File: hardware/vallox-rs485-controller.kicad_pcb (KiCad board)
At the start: 0 parts

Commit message: hw(pcb): rev A placement on a 104 x 66 mm board, not yet routed
The board file was empty. All 60 schematic parts are now on the top side,
placed from the netlist with KiCad's bundled pcbnew Python (KiCad closed):
the MCP server had no pcb_write tools this session and the file-based MCP
transfer tool is the one the workspace forbids. Every footprint carries its
symbol UUID as path, so a GUI F8 should reconcile to no changes.

Floor plan: display glass reserve top-left with the four buttons centred
under it and the LEDs beside it; FPC connector on the glass's short edge;
ESP32 module top-right with its antenna 6 mm over the edge, the position the
Espressif hardware design guide recommends; terminal block and USB-C flush
with the right edge so all field wiring enters from one wall; buck in the
bottom-right corner, RS-485 front end between terminal and module.

kicad-cli drc --severity-all --schematic-parity: 0 errors, 7 warnings
(silkscreen of edge-mounted U1/J1/J2 crossing the edge; U1 thermal vias
widened from 0.2 to 0.3 mm drill to meet the project's min-hole rule),
parity clean apart from the four intentional mounting holes, 138 unconnected
items because nothing is routed. Parity caught two build mistakes on the way:
footprints written without their library nickname, and TP1/TP2/JP1 symbols
not excluded from BOM while their footprints are — the symbols now say
in_bom no, ERC unchanged.

CI's DRC step will stay red on this branch until the board is routed:
--exit-code-violations also counts unconnected items (verified locally).
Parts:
- added C1: 220u/35V, Capacitor_SMD:CP_Elec_8x10.5, F.Cu at (80.0, 58.5)
- added C10: 10u, Capacitor_SMD:C_0603_1608Metric, F.Cu at (80.3, 2.20)
- added C11: 100n, Capacitor_SMD:C_0603_1608Metric, F.Cu at (75.5, 2.20)
- added C12: 100n, Capacitor_SMD:C_0603_1608Metric, F.Cu at (80.3, 13.4)
- added C13: 1u, Capacitor_SMD:C_0603_1608Metric, F.Cu at (80.3, 7.80)
- added C2: 2.2u/50V, Capacitor_SMD:C_0805_2012Metric, F.Cu at (79.8, 50.2)
- added C3: 100n, Capacitor_SMD:C_0603_1608Metric, F.Cu at (85.6, 47.6)
- added C4: 22u/10V, Capacitor_SMD:C_0805_2012Metric, F.Cu at (69.0, 48.6)
- added C5: 22u/10V, Capacitor_SMD:C_0805_2012Metric, F.Cu at (69.0, 52.2)
- added C7: 10u, Capacitor_SMD:C_0603_1608Metric, F.Cu at (72.8, 42.5)
- added C8: 100n, Capacitor_SMD:C_0603_1608Metric, F.Cu at (84.8, 38.6)
- added C9: 1u, Capacitor_SMD:C_0603_1608Metric, F.Cu at (73.5, 24.5)
- added D1: SS34, Diode_SMD:D_SMA, F.Cu at (89.9, 59.5)
- added D2: SM712, Package_TO_SOT_SMD:SOT-23, F.Cu at (90.8, 36.0)
- added D3: SS34, Diode_SMD:D_SMA, F.Cu at (89.5, 32.4)
- added D4: PWR, LED_SMD:LED_0603_1608Metric, F.Cu at (63.8, 10.0)
- added D5: FAULT, LED_SMD:LED_0603_1608Metric, F.Cu at (63.8, 18.0)
- added D6: BUS, LED_SMD:LED_0603_1608Metric, F.Cu at (63.8, 14.0)
- added F1: 100mA/60V, Fuse:Fuse_1812_4532Metric, F.Cu at (90.2, 45.6)
- added F2: 100mA/60V, Fuse:Fuse_1812_4532Metric, F.Cu at (90.2, 39.9)
- added H1: M3, MountingHole:MountingHole_3.2mm_M3, F.Cu at (3.50, 3.50)
- added H2: M3, MountingHole:MountingHole_3.2mm_M3, F.Cu at (3.50, 62.5)
- added H3: M3, MountingHole:MountingHole_3.2mm_M3, F.Cu at (100.5, 62.5)
- added H4: M3, MountingHole:MountingHole_3.2mm_M3, F.Cu at (70.0, 3.50)
- added J1: + - A B M, TerminalBlock_Phoenix:TerminalBlock_Phoenix_MKDS-1,5-5-5.08_1x05_P5.08mm_Horizontal, F.Cu at (99.4, 55.5)
- added J2: TYPE-C-31-M-12, Connector_USB:USB_C_Receptacle_HRO_TYPE-C-31-M-12, F.Cu at (100.3, 26.0)
- added J3: HS20HS072RX, Connector_FFC-FPC:Hirose_FH12-12S-0.5SH_1x12-1MP_P0.50mm_Horizontal, F.Cu at (67.0, 26.1)
- added JP1: TERM, Jumper:SolderJumper-2_P1.3mm_Open_RoundedPad1.0x1.5mm, F.Cu at (82.6, 35.0)
- added L1: 22uH, Inductor_SMD:L_Changjiang_FNR6045S, F.Cu at (74.5, 50.2)
- added Q1: AO3400A, Package_TO_SOT_SMD:SOT-23, F.Cu at (73.5, 30.5)
- added R1: 100k, Resistor_SMD:R_0603_1608Metric, F.Cu at (89.0, 52.5)
- added R10: 10k, Resistor_SMD:R_0603_1608Metric, F.Cu at (73.5, 22.3)
- added R11: 27R, Resistor_SMD:R_1206_3216Metric, F.Cu at (73.5, 34.2)
- added R12: 100R, Resistor_SMD:R_0603_1608Metric, F.Cu at (77.5, 29.5)
- added R13: 10k, Resistor_SMD:R_0603_1608Metric, F.Cu at (77.5, 31.5)
- added R14: 5.1k, Resistor_SMD:R_0603_1608Metric, F.Cu at (92.5, 28.5)
- added R15: 5.1k, Resistor_SMD:R_0603_1608Metric, F.Cu at (92.5, 23.5)
- added R19: 10k, Resistor_SMD:R_0603_1608Metric, F.Cu at (80.3, 5.00)
- added R2: 15k, Resistor_SMD:R_0603_1608Metric, F.Cu at (89.0, 50.8)
- added R20: 1k, Resistor_SMD:R_0603_1608Metric, F.Cu at (67.3, 10.0)
- added R21: 10k, Resistor_SMD:R_0603_1608Metric, F.Cu at (73.5, 26.7)
- added R22: 10k, Resistor_SMD:R_0603_1608Metric, F.Cu at (80.3, 10.6)
- added R23: 1.5k, Resistor_SMD:R_0603_1608Metric, F.Cu at (27.5, 58.5)
- added R24: 3.3k, Resistor_SMD:R_0603_1608Metric, F.Cu at (40.5, 58.5)
- added R25: 6.8k, Resistor_SMD:R_0603_1608Metric, F.Cu at (53.5, 58.5)
- added R26: 1k, Resistor_SMD:R_0603_1608Metric, F.Cu at (67.3, 18.0)
- added R27: 1k, Resistor_SMD:R_0603_1608Metric, F.Cu at (67.3, 14.0)
- added R3: 100k, Resistor_SMD:R_0603_1608Metric, F.Cu at (89.0, 55.9)
- added R4: 13.3k, Resistor_SMD:R_0603_1608Metric, F.Cu at (89.0, 54.2)
- added R5: 120R DNP, Resistor_SMD:R_0603_1608Metric, F.Cu at (79.2, 35.0)
- added R6: 1k DNP, Resistor_SMD:R_0603_1608Metric, F.Cu at (78.4, 38.6)
- added R7: 1k DNP, Resistor_SMD:R_0603_1608Metric, F.Cu at (81.6, 38.6)
- added R8: 10k, Resistor_SMD:R_0603_1608Metric, F.Cu at (75.5, 7.60)
- added R9: 10k, Resistor_SMD:R_0603_1608Metric, F.Cu at (75.5, 10.4)
- added SW1: -, Button_Switch_SMD:SW_SPST_PTS645Sx43SMTR92, F.Cu at (14.5, 52.0)
- added SW2: +, Button_Switch_SMD:SW_SPST_PTS645Sx43SMTR92, F.Cu at (27.5, 52.0)
- added SW3: OK, Button_Switch_SMD:SW_SPST_PTS645Sx43SMTR92, F.Cu at (40.5, 52.0)
- added SW4: BACK, Button_Switch_SMD:SW_SPST_PTS645Sx43SMTR92, F.Cu at (53.5, 52.0)
- added TP1: EN, TestPoint:TestPoint_Pad_1.0x1.0mm, F.Cu at (75.5, 4.80)
- added TP2: BOOT, TestPoint:TestPoint_Pad_1.0x1.0mm, F.Cu at (77.6, 13.0)
- added U1: ESP32-C3-WROOM-02-N4, RF_Module:ESP32-C3-WROOM-02, F.Cu at (92.0, 7.10)
- added U2: TPS54202DDC, Package_TO_SOT_SMD:SOT-23-6, F.Cu at (83.5, 50.2)
- added U3: ME6211C33M5G-N, Package_TO_SOT_SMD:SOT-23-5, F.Cu at (69.0, 43.5)
- added U4: THVD1400DR, Package_SO:SOIC-8_3.9x4.9mm_P1.27mm, F.Cu at (82.5, 42.8)
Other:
- board outline added: 104 x 66 mm
- copper layers 0 -> 2
- board text added: "+"
- board text added: "-"
- board text added: "A"
- board text added: "B"
- board text added: "BACK"
- board text added: "BUS"
- board text added: "FAULT"
- board text added: "FPC tail assumed to exit the right (short) edge toward J3 - verify from the display drawing."
- board text added: "HS20HS072RX glass 51.8 x 36.2 mm - component-free area (glass rests on the board)."
- board text added: "Keep enclosure metal >= 15 mm from the antenna."
- board text added: "M"
- board text added: "OK"
- board text added: "PWR"
- board text added: "U1 antenna overhangs the board edge by 6 mm (Espressif HDG preferred position)."
- board text added: "VALLOX RS-485 CONTROLLER rev A"
- board text added: "mironet.fi github.com/Miroeilola/vallox-rs485-controller"

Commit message: hw(display): place DS1 glass from the shared library, move the LEDs off the FPC tail
The shared library now has an own model of the HS20HS072RX and a pad-less
footprint for it, so the reserved rectangle becomes a real part on the board.
The first render with the glass in place showed the 20.6 mm wide tail root
lying across the FAULT LED and its legend; the LED column moves up three
millimetres and one mounting hole moves left to make room. DRC and schematic
parity unchanged (0 errors; the four holes are the only extras), 138 items
still unrouted.

Also fixes the model path on the placed footprint: the library convention
resolved relative to the KiCad project directory, which in this layout is
hardware/, not the repository root where the submodule lives.
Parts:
- added DS1: HS20HS072RX, mironet:LCD_2.0in_HSD_HS20HS072RX_FPC-12P-0.5mm, F.Cu at (33.9, 26.1)
- moved D5 4.20 mm to (63.8, 13.8)
- moved R26 4.20 mm to (67.3, 13.8)
- moved H4 4.00 mm to (66.0, 3.50)
- moved D6 3.20 mm to (63.8, 10.8)
- moved R27 3.20 mm to (67.3, 10.8)
- moved D4 2.20 mm to (63.8, 7.80)
- moved R20 2.20 mm to (67.3, 7.80)
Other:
- board text added: "DS1 glass rests on the board; tail contact side unverified (drawing: viewer side) - decides whether J3 turns 180 deg"
- board text removed: "FPC tail assumed to exit the right (short) edge toward J3 - verify from the display drawing."
- board text removed: "HS20HS072RX glass 51.8 x 36.2 mm - component-free area (glass rests on the board)."
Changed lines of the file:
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@@
 	(footprint "Resistor_SMD:R_0603_1608Metric"
 		(layer "F.Cu")
-		(at 67.3 18)
+		(at 67.3 13.8)
 		(descr "Resistor SMD 0603 (1608 Metric), square (rectangular) end terminal, IPC-7351 nominal, (Body size source: IPC-SM-782 page 72, https://www.pcb-3d.com/wordpress/wp-content/uploads/ipc-sm-782a_amendment_1_and_2.pdf)")
 		(tags "resistor")
 		(property "Reference" "R26"
-			(at 0 -1.7036 0)
+			(at 0 1.7036 0)
 			(layer "F.SilkS")
 			(effects
@@
 	(footprint "Resistor_SMD:R_0603_1608Metric"
 		(layer "F.Cu")
-		(at 67.3 14)
+		(at 67.3 10.8)
 		(descr "Resistor SMD 0603 (1608 Metric), square (rectangular) end terminal, IPC-7351 nominal, (Body size source: IPC-SM-782 page 72, https://www.pcb-3d.com/wordpress/wp-content/uploads/ipc-sm-782a_amendment_1_and_2.pdf)")
 		(tags "resistor")
@@
 		(tags "capacitor")
 		(property "Reference" "C11"
-			(at 2.4536 0 90)
+			(at 3.036905 0 0)
 			(layer "F.SilkS")
 			(effects
@@
 	(footprint "LED_SMD:LED_0603_1608Metric"
 		(layer "F.Cu")
-		(at 63.8 14)
+		(at 63.8 10.8)
 		(descr "LED SMD 0603 (1608 Metric), square (rectangular) end terminal, IPC-7351 nominal, (Body size source: http://www.tortai-tech.com/upload/download/2011102023233369053.pdf)")
 		(tags "LED")
 		(property "Reference" "D6"
-			(at 0 -1.7036 0)
+			(at -2.4536 0 90)
 			(layer "F.SilkS")
 			(effects
@@
 	(footprint "LED_SMD:LED_0603_1608Metric"
 		(layer "F.Cu")
-		(at 63.8 18)
+		(at 63.8 13.8)
 		(descr "LED SMD 0603 (1608 Metric), square (rectangular) end terminal, IPC-7351 nominal, (Body size source: http://www.tortai-tech.com/upload/download/2011102023233369053.pdf)")
 		(tags "LED")
 		(property "Reference" "D5"
-			(at 0 -1.7036 0)
+			(at 0 1.7036 0)
 			(layer "F.SilkS")
 			(effects
@@
 	(footprint "LED_SMD:LED_0603_1608Metric"
 		(layer "F.Cu")
-		(at 63.8 10)
+		(at 63.8 7.8)
 		(descr "LED SMD 0603 (1608 Metric), square (rectangular) end terminal, IPC-7351 nominal, (Body size source: http://www.tortai-tech.com/upload/download/2011102023233369053.pdf)")
 		(tags "LED")
 		(property "Reference" "D4"
-			(at 0 -1.7036 0)
+			(at -2.4536 0 90)
 			(layer "F.SilkS")
 			(effects
@@
 	(footprint "MountingHole:MountingHole_3.2mm_M3"
 		(layer "F.Cu")
-		(at 70 3.5)
+		(at 66 3.5)
 		(descr "Mounting Hole 3.2mm, M3, no annular, generated by kicad-footprint-generator mountinghole.py")
 		(tags "mountinghole M3")
@@
 		)
 	)
+	(footprint "mironet:LCD_2.0in_HSD_HS20HS072RX_FPC-12P-0.5mm"
+		(layer "F.Cu")
+		(at 33.9 26.1 90)
+		(descr "HSD HS20HS072RX 2.0in 320x240 IPS TFT, ST7789, 12-pin 0.5 mm FPC tail; glass outline 36.2x51.8x2.05 mm, VA 33.6x46.6 (recommended window), AA 30.6x40.8; mechanical footprint, no pads; from the manufacturer outline drawing (general tolerance +-0.2 mm)")
+		(tags "display TFT IPS ST7789 HS20HS072RX LCD 2.0in")
+		(property "Reference" "DS1"
+			(at 0 -27.4 90)
+			(layer "F.Fab")
+			(hide yes)
+			(effects
+				(font
+					(size 1 1)
+				)
+			)
+		)
+		(property "Value" "HS20HS072RX"
+			(at 0 20.4 90)
+			(layer "F.Fab")
+			(effects
+				(font
+					(size 1 1)
+				)
+			)
+		)
+		(property "Datasheet" ""
+			(at 0 0 90)
+			(layer "F.Fab")
+			(hide yes)
+			(effects
+				(font
+					(size 1.27 1.27)
+				)
+			)
+		)
+		(property "Description" ""
+			(at 0 0 90)
+			(layer "F.Fab")
+			(hide yes)
+			(effects
+				(font
+					(size 1.27 1.27)
+				)
+			)
+		)
+		(attr board_only exclude_from_pos_files exclude_from_bom)
+		(duplicate_pad_numbers_are_jumpers no)
+		(fp_line
+			(start -4.07 47.399999)
+			(end -2.07 47.399999)
+			(stroke
+				(width 0.12)
+				(type default)
+			)
+			(layer "F.SilkS")
+		)
+		(fp_rect
+			(start -16.8 -24.599999)
+			(end 16.8 22)
+			(stroke
+				(width 0.12)
+				(type default)
+			)
+			(fill no)
+			(layer "Dwgs.User")
+		)
+		(fp_rect
+			(start -15.3 -23.259999)
+			(end 15.3 17.54)
+			(stroke
+				(width 0.12)
+				(type default)
+			)
+			(fill no)
+			(layer "Dwgs.User")
+		)
+		(fp_rect
+			(start -18.6 -26.4)
+			(end 18.6 26.4)
+			(stroke
+				(width 0.05)
+				(type default)
+			)
+			(fill no)
+			(layer "F.CrtYd")
+		)
+		(fp_rect
+			(start -11 25.9)
+			(end 10.599999 36.2)
+			(stroke
+				(width 0.05)
+				(type default)
+			)
+			(fill no)
+			(layer "F.CrtYd")
+		)
+		(fp_rect
+			(start -3.57 35.7)
+			(end 3.929999 47.099999)
+			(stroke
+				(width 0.05)
+				(type default)
+			)
+			(fill no)
+			(layer "F.CrtYd")
+		)
+		(fp_rect
+			(start -18.1 -25.9)
+			(end 18.1 25.9)
+			(stroke
+				(width 0.1)
+				(type default)
+			)
+			(fill no)
+			(layer "F.Fab")
+		)
+		(fp_poly
+			(pts
+				(xy -10.5 25.9) (xy -10.5 35.7) (xy -3.07 35.7) (xy -3.07 46.599999) (xy 3.429999 46.599999) (xy 3.429999 35.7)
+				(xy 10.099999 35.7) (xy 10.099999 25.9)
+			)
+			(stroke
+				(width 0.1)
+				(type default)
+			)
+			(fill no)
+			(layer "F.Fab")
+		)
+		(fp_text user "AA 30.6x40.8"
+			(at 0 -22.259999 90)
+			(layer "Dwgs.User")
+			(effects
+				(font
+					(size 0.7 0.7)
+					(thickness 0.105)
+				)
+			)
+		)
+		(fp_text user "VA 33.6x46.6 = window"
+			(at 0 20.8 90)
+			(layer "Dwgs.User")
+			(effects
+				(font
+					(size 0.7 0.7)
+					(thickness 0.105)
+				)
+			)
+		)
+		(fp_text user "12P 0.5mm"
+			(at 0.179999 45.099999 90)
+			(layer "Dwgs.User")
+			(effects
+				(font
+					(size 0.6 0.6)
+					(thickness 0.09)
+				)
+			)
+		)
+		(embedded_fonts no)
+		(model "${KIPRJMOD}/../lib/mironet-hw-lib/3dmodels/LCD_2.0in_HSD_HS20HS072RX.step"
+			(offset
+				(xyz 0 0 0)
+			)
+			(scale
+				(xyz 1 1 1)
+			)
+			(rotate
+				(xyz 0 0 0)
+			)
+		)
+	)
 	(footprint "Resistor_SMD:R_1206_3216Metric"
 		(layer "F.Cu")
@@
 		(tags "resistor")
 		(property "Reference" "R8"
-			(at -2.655952 0 0)
+			(at -2.4536 0 90)
 			(layer "F.SilkS")
 			(effects
@@
 	(footprint "Resistor_SMD:R_0603_1608Metric"
 		(layer "F.Cu")
-		(at 67.3 10)
+		(at 67.3 7.8)
 		(descr "Resistor SMD 0603 (1608 Metric), square (rectangular) end terminal, IPC-7351 nominal, (Body size source: IPC-SM-782 page 72, https://www.pcb-3d.com/wordpress/wp-content/uploads/ipc-sm-782a_amendment_1_and_2.pdf)")
 		(tags "resistor")
@@
 		)
 	)
-	(gr_rect
-		(start 8 8)
-		(end 59.8 44.2)
-		(stroke
-			(width 0.15)
-			(type default)
-		)
-		(fill no)
-		(layer "Dwgs.User")
-	)
 	(gr_arc
 		(start 0 2)
@@
 	)
 	(gr_text "PWR"
-		(at 70.6 10 0)
+		(at 70.6 7.8 0)
 		(layer "F.SilkS")
 		(effects
@@
 	)
 	(gr_text "BUS"
-		(at 70.6 14 0)
+		(at 70.6 10.8 0)
 		(layer "F.SilkS")
 		(effects
@@
 	)
 	(gr_text "FAULT"
-		(at 71 18 0)
+		(at 71 13.8 0)
 		(layer "F.SilkS")
 		(effects
@@
 		)
 	)
-	(gr_text "U1 antenna overhangs the board edge by 6 mm (Espressif HDG preferred position)."
-		(at 86.5 15.7 0)
+	(gr_text "DS1 glass rests on the board; tail contact side unverified (drawing: viewer side) - decides whether J3 turns 180 deg"
+		(at 33.9 46 0)
 		(layer "Cmts.User")
 		(effects
@@
 		)
 	)
-	(gr_text "Keep enclosure metal >= 15 mm from the antenna."
-		(at 86.5 16.8 0)
+	(gr_text "U1 antenna overhangs the board edge by 6 mm (Espressif HDG preferred position)."
+		(at 86.5 15.7 0)
 		(layer "Cmts.User")
 		(effects
@@
 		)
 	)
-	(gr_text "HS20HS072RX glass 51.8 x 36.2 mm - component-free area (glass rests on the board)."
-		(at 33.9 25 0)
-		(layer "Cmts.User")
-		(effects
-			(font
-				(size 0.7 0.7)
-				(thickness 0.105)
-			)
-		)
-	)
-	(gr_text "FPC tail assumed to exit the right (short) edge toward J3 - verify from the display drawing."
-		(at 33.9 26.4 0)
+	(gr_text "Keep enclosure metal >= 15 mm from the antenna."
+		(at 86.5 16.8 0)
 		(layer "Cmts.User")
 		(effects
 			(font
-				(size 0.7 0.7)
-				(thickness 0.105)
+				(size 0.6 0.6)
+				(thickness 0.09)
 			)
 		)

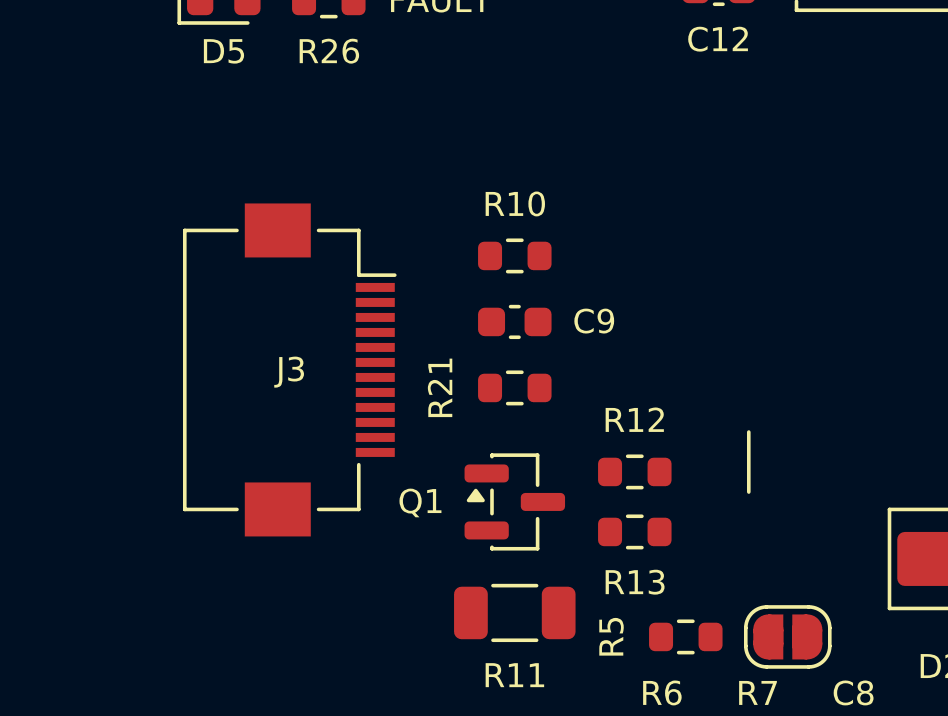
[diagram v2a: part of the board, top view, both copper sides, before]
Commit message: hw(display): fold the tail over J3 — contacts face the viewer, so J3 turns 180°
LCSC's part photos settle the contact side: gold fingers and LED test pads on
the viewer face, stiffener on the back. A bottom-contact FH12 therefore takes
the tail folded over it, entering from the side away from the glass. J3 turns
round with its entry face 9.5 mm from the glass edge, placed so that pin 1
meets tail contact 1; DS1 becomes the library's folded-tail variant so the
3D export and the enclosure see the loop, and one passive column moves out
from under it. DRC and parity unchanged.
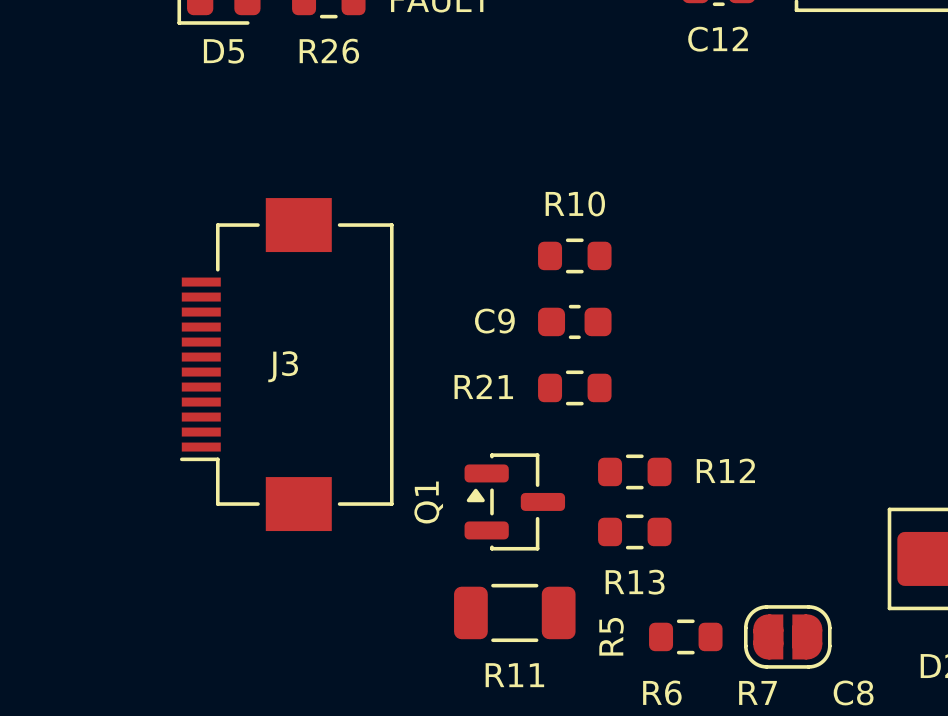
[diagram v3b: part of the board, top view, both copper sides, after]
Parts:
- DS1: footprint mironet:LCD_2.0in_HSD_HS20HS072RX_FPC-12P-0.5mm -> mironet:LCD_2.0in_HSD_HS20HS072RX_FPC-12P-0.5mm_TailFolded
- moved J3 2.11 mm to (64.9, 25.9), turned to 90 degrees
- moved C9 2.00 mm to (75.5, 24.5)
- moved R10 2.00 mm to (75.5, 22.3)
- moved R21 2.00 mm to (75.5, 26.7)
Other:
- board text added: "DS1 glass rests on the board. Tail contacts face the viewer (verified from part photos): tail folds 180 deg over J3 and enters from the right; J3 entry face 9.5 mm from the glass edge."
- board text removed: "DS1 glass rests on the board; tail contact side unverified (drawing: viewer side) - decides whether J3 turns 180 deg"

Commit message: hw(display): straight tail into a top-contact FH12A; J3 mirrored in the schematic
The fold would have lifted the FPC loop above the glass and cost a manual
step per unit. With the contact side known, a top-contact connector takes
the tail straight: Hirose FH12A-12S-0.5SH(55) shares the FH12 land pattern
(catalogue p. 10), so the footprint and model stay; J3 moves east so its
entry face is 16.9 mm from the glass edge and DS1 carries the straight model.

Straight insertion puts tail contact k on the pad the footprint numbers
13-k — a fact of coordinates, verified on the board (pad 11 = CS meets
contact 2 at y 28.17) — so the schematic symbol is mirrored and the mapping
written out pin by pin. ERC unchanged, netlist checked, board pad nets
re-synced, DRC 0 errors / 7 known warnings, schematic parity clean.
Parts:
- DS1: footprint mironet:LCD_2.0in_HSD_HS20HS072RX_FPC-12P-0.5mm_TailFolded -> mironet:LCD_2.0in_HSD_HS20HS072RX_FPC-12P-0.5mm
- J3: value HS20HS072RX -> FH12A-12S-0.5SH(55)
- moved J3 7.40 mm to (72.3, 25.9), turned to -90 degrees
- moved Q1 3.40 mm to (73.5, 33.9)
- moved C9 3.00 mm to (78.5, 24.5)
- moved R10 3.00 mm to (78.5, 22.3)
- moved R11 3.00 mm to (73.5, 37.2)
- moved R21 3.00 mm to (78.5, 26.7)
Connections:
- J3 pad 10: Net-(J3-Pin_10) -> /TFT_DC
- J3 pad 11: /TFT_LED_K -> /TFT_CS
- J3 pad 2: /TFT_CS -> /TFT_LED_K
- J3 pad 3: /TFT_DC -> Net-(J3-Pin_3)
- J3 pad 4: /TFT_SCK -> +3V3
- J3 pad 5: /TFT_MOSI -> +3V3
- J3 pad 6: /TFT_RST -> unconnected-(J3-Pin_6-Pad6)
- J3 pad 7: unconnected-(J3-Pin_7-Pad7) -> /TFT_RST
- J3 pad 8: +3V3 -> /TFT_MOSI
- J3 pad 9: +3V3 -> /TFT_SCK
- R11 pad 2: Net-(J3-Pin_10) -> Net-(J3-Pin_3)
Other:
- board text added: "DS1 glass rests on the board. Tail contacts face the viewer; J3 is a TOP-contact FH12A facing the glass, tail straight, entry 16.9 mm from the glass edge. Keep the tail path (y 23-29, x 60-77) below 0.8 mm."
- board text removed: "DS1 glass rests on the board. Tail contacts face the viewer (verified from part photos): tail folds 180 deg over J3 and enters from the right; J3 entry face 9.5 mm from the glass edge."
